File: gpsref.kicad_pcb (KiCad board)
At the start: 4 copper layers, 77.4 x 47.8 mm, 182 parts, among them J1 SMA, J11 Debug, J12 GPS_Snoop, J13 I2C_Snoop, J2 SMA, J3 SMA, J4 SMA, J5 U.Fl, J6 SMA, J7 USB_C_Receptacle_16P, Q1 AO3400A, Q2 AO3401A, T1 MABA-007159-000000, T2 MABA-007159-000000, U1 MAX-M10S, U12 74LVC1G125, U13 74CB3Q3306, U15 74LVC1G07, U2 TG5032CGN, U3 LMK05318BRGZR, U31 TMP117xxDRV, U4 STM32H503KBUx, U5 TPS82084SIL, U6 TPS82084SIL, U7 TPS7A8801RTJR, U9 TPS7A8801RTJR, Y1 32768Hz

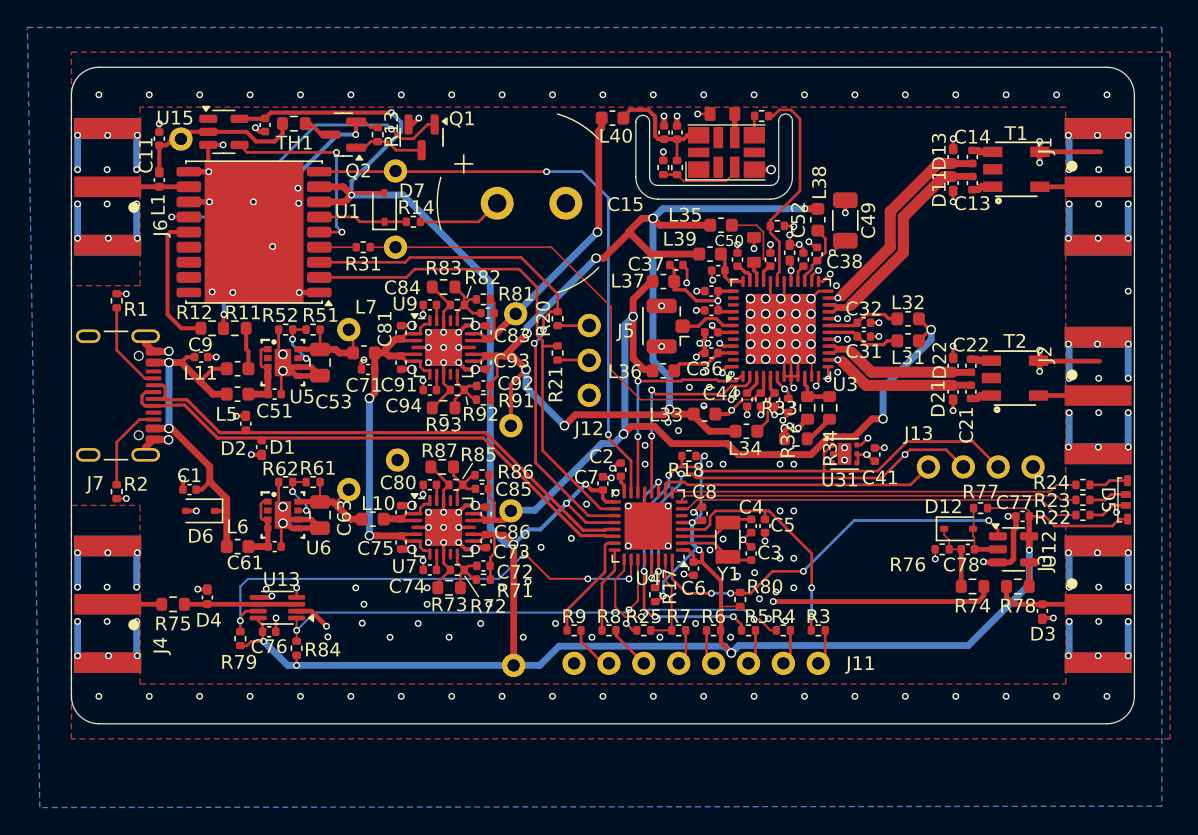
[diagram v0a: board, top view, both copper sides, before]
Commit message: Squeeze in a connector to break out GPS.
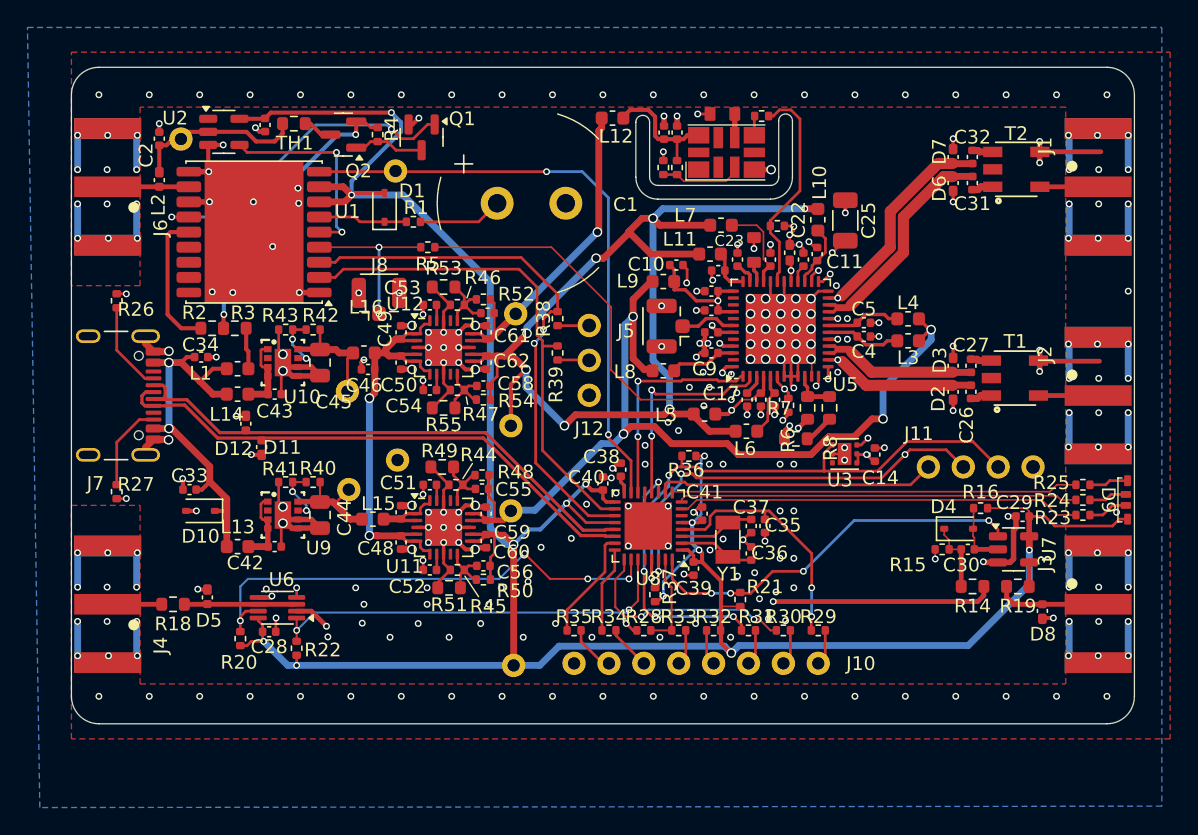
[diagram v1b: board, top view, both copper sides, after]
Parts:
- removed TP13: TestPoint_Probe, Parts:TestPoint
- added J8: U.Fl, Parts:U.FL_Hirose_U.FL-R-SMT-1_Vertical, F.Cu at (122.4, 93.0)
- moved R5 4.70 mm to (126.0, 89.2)
- moved TP5 4.50 mm to (120.1, 99.7)
- renumbered C15 to C1, C37 to C10, C38 to C11, C39 to C12, C40 to C13, C41 to C14, C42 to C15, C43 to C16, C44 to C17, C45 to C18, C46 to C19, C11 to C2, C47 to C20, C48 to C21, C52 to C22, C50 to C23, C56 to C24, C49 to C25, C21 to C26, C22 to C27, C76 to C28, C77 to C29, C12 to C3, C78 to C30, C13 to C31, C14 to C32, C1 to C33, C9 to C34, C5 to C35, C3 to C36, C4 to C37, C2 to C38, C6 to C39, C31 to C4, C7 to C40, C8 to C41, C61 to C42, C51 to C43, C63 to C44, C53 to C45, C71 to C46, C79 to C47, C75 to C48, C81 to C49, C32 to C5, C91 to C50, C80 to C51, C74 to C52, C84 to C53, C94 to C54, C85 to C55, C72 to C56, C82 to C57, C92 to C58, C86 to C59, C33 to C6, C73 to C60, C83 to C61, C93 to C62, C34 to C7, C35 to C8, C36 to C9, D7 to D1, D6 to D10, D1 to D11, D2 to D12, D21 to D2, D22 to D3, D12 to D4, D4 to D5, D11 to D6, D13 to D7, D3 to D8, D5 to D9, J11 to J10, J13 to J11, L11 to L1, L38 to L10, L39 to L11, L40 to L12, L6 to L13, L5 to L14, L10 to L15, L7 to L16, L1 to L2, L31 to L3, L32 to L4, L33 to L5, L34 to L6, L35 to L7, L36 to L8, L37 to L9, R14 to R1, R37 to R10, R38 to R11, R40 to R12, R39 to R13, R74 to R14, R76 to R15, R77 to R16, R75 to R18, R78 to R19, R12 to R2, R79 to R20, R80 to R21, R84 to R22, R22 to R23, R23 to R24, R24 to R25, R1 to R26, R2 to R27, R25 to R28, R3 to R29, R11 to R3, R4 to R30, R5 to R31, R6 to R32, R7 to R33, R8 to R34, R9 to R35, R18 to R36, R17 to R37, R20 to R38, R21 to R39, R13 to R4, R61 to R40, R62 to R41, R51 to R42, R52 to R43, R85 to R44, R72 to R45, R82 to R46, R92 to R47, R86 to R48, R87 to R49, R31 to R5, R71 to R50, R73 to R51, R81 to R52, R83 to R53, R91 to R54, R93 to R55, R32 to R6, R33 to R7, R34 to R8, R35 to R9, T2 to T1, T1 to T2, TP12 to TP1, TP14 to TP2, TP4 to TP3, TP6 to TP4, TP10 to TP6, U5 to U10, U7 to U11, U9 to U12, U15 to U2, U31 to U3, U2 to U4, U3 to U5, U13 to U6, U12 to U7, U4 to U8, U6 to U9
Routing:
- net GPSCLK: track 2.69 -> 12.2 mm, vias 0 -> 2
- net /Clocking/GPSCLKLO: track 39.7 -> 35.0 mm
- net /Power/3V6: track 7.22 -> 8.50 mm
- net GND: track 214.2 -> 214.4 mm, vias 300 -> 302

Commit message: Tweak positioning.
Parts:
- moved J7 0.50 mm to (102.8, 100.0)
- moved R26 0.50 mm to (103.8, 93.1)
- moved R27 0.50 mm to (103.8, 107.0)
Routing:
- net /CPU/USB_D-: track 40.0 -> 39.5 mm
- net /CPU/USB_D+: track 40.0 -> 39.5 mm
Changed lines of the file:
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@@
 	(footprint "Resistor_SMD:R_0402_1005Metric"
 		(layer "F.Cu")
-		(at 103.3 93.1 -90)
+		(at 103.8 93.1 -90)
 		(descr "Resistor SMD 0402 (1005 Metric), square (rectangular) end terminal, IPC-7351 nominal, (Body size source: IPC-SM-782 page 72, https://www.pcb-3d.com/wordpress/wp-content/uploads/ipc-sm-782a_amendment_1_and_2.pdf), generated with kicad-footprint-generator")
 		(tags "resistor")
@@
 	(footprint "Resistor_SMD:R_0402_1005Metric"
 		(layer "F.Cu")
-		(at 103.3 107 90)
+		(at 103.8 107 90)
 		(descr "Resistor SMD 0402 (1005 Metric), square (rectangular) end terminal, IPC-7351 nominal, (Body size source: IPC-SM-782 page 72, https://www.pcb-3d.com/wordpress/wp-content/uploads/ipc-sm-782a_amendment_1_and_2.pdf), generated with kicad-footprint-generator")
 		(tags "resistor")
@@
 		(locked yes)
 		(layer "F.Cu")
-		(at 102.3 100 -90)
+		(at 102.8 100 -90)
 		(descr "USB 2.0 Type C Receptacle, GCT, 16P, top mounted, horizontal, 5A: https://gct.co/files/drawings/usb4105.pdf")
 		(tags "USB C Type-C Receptacle SMD USB 2.0 16P 16C USB4105-15-A USB4105-15-A-060 USB4105-15-A-120 USB4105-GF-A USB4105-GF-A-060 USB4105-GF-A-120")
@@
 	)
 	(segment
-		(start 107.074228 103.2246)
-		(end 107.049628 103.2)
+		(start 107.574228 103.2246)
+		(end 107.549628 103.2)
 		(width 0.5)
 		(layer "F.Cu")
@@
 	)
 	(segment
-		(start 107.049628 103.2)
-		(end 105.98 103.2)
+		(start 107.549628 103.2)
+		(end 106.48 103.2)
 		(width 0.5)
 		(layer "F.Cu")
@@
 	)
 	(segment
-		(start 105.405 103.775)
-		(end 105.405 104.32)
+		(start 105.905 103.775)
+		(end 105.905 104.32)
 		(width 0.5)
 		(layer "F.Cu")
@@
 	)
 	(segment
-		(start 103.99 92.59)
-		(end 104 92.6)
+		(start 104.49 92.59)
+		(end 104.5 92.6)
 		(width 0.2)
 		(layer "F.Cu")
@@
 	)
 	(segment
-		(start 103.99 107.51)
-		(end 104 107.5)
+		(start 104.49 107.51)
+		(end 104.5 107.5)
 		(width 0.2)
 		(layer "F.Cu")
@@
 	)
 	(segment
-		(start 103.3 107.51)
-		(end 103.99 107.51)
+		(start 103.8 107.51)
+		(end 104.49 107.51)
 		(width 0.2)
 		(layer "F.Cu")
@@
 	)
 	(segment
-		(start 105.98 96.8)
-		(end 107.074997 96.8)
+		(start 106.48 96.8)
+		(end 107.574997 96.8)
 		(width 0.5)
 		(layer "F.Cu")
@@
 	)
 	(segment
-		(start 105.405 96.225)
-		(end 105.405 95.68)
+		(start 105.905 96.225)
+		(end 105.905 95.68)
 		(width 0.5)
 		(layer "F.Cu")
@@
 	)
 	(segment
-		(start 105.98 103.2)
-		(end 105.405 103.775)
+		(start 106.48 103.2)
+		(end 105.905 103.775)
 		(width 0.5)
 		(layer "F.Cu")
@@
 	)
 	(segment
-		(start 105.98 96.8)
-		(end 105.405 96.225)
+		(start 106.48 96.8)
+		(end 105.905 96.225)
 		(width 0.5)
 		(layer "F.Cu")
@@
 	)
 	(segment
-		(start 107.074997 96.8)
-		(end 107.1 96.774997)
+		(start 107.574997 96.8)
+		(end 107.6 96.774997)
 		(width 0.5)
 		(layer "F.Cu")
@@
 	)
 	(segment
-		(start 103.3 92.59)
-		(end 103.99 92.59)
+		(start 103.8 92.59)
+		(end 104.49 92.59)
 		(width 0.2)
 		(layer "F.Cu")
@@
 	)
 	(via
-		(at 107.074228 103.2246)
+		(at 107.574228 103.2246)
 		(size 0.7)
 		(drill 0.5)
@@
 	)
 	(via
-		(at 107.1 96.774997)
+		(at 107.6 96.774997)
 		(size 0.7)
 		(drill 0.5)
@@
 	)
 	(via
-		(at 104 92.6)
+		(at 104.5 92.6)
 		(size 0.5)
 		(drill 0.3)
@@
 	)
 	(via
-		(at 104 107.5)
+		(at 104.5 107.5)
 		(size 0.5)
 		(drill 0.3)
@@
 	)
 	(segment
-		(start 107.1 97.6)
-		(end 105.98 97.6)
+		(start 107.6 97.6)
+		(end 106.48 97.6)
 		(width 0.5)
 		(layer "F.Cu")
@@
 	)
 	(segment
-		(start 107.1 102.4)
-		(end 107.3 102.4)
+		(start 108 102.4)
+		(end 110.075 104.475)
+		(width 0.5)
+		(layer "F.Cu")
+		(net 2)
+	)
+	(segment
+		(start 110.075 104.475)
+		(end 110.075 106.275)
 		(width 0.5)
 		(layer "F.Cu")
@@
 	)
 	(segment
-		(start 109.375 98.975)
-		(end 110.3 99.9)
+		(start 107.1 102.4)
+		(end 108 102.4)
 		(width 0.5)
 		(layer "F.Cu")
@@
 	)
 	(segment
-		(start 108.4 97.2)
-		(end 108 97.6)
-		(width 0.3)
-		(layer "F.Cu")
-		(net 2)
-	)
-	(segment
-		(start 110.075 105.175)
-		(end 110.075 106.275)
+		(start 109.375 98.975)
+		(end 110.3 99.9)
 		(width 0.5)
 		(layer "F.Cu")
@@
 	)
 	(segment
-		(start 107.3 102.4)
-		(end 110.075 105.175)
-		(width 0.5)
+		(start 108.4 97.2)
+		(end 108 97.6)
+		(width 0.3)
 		(layer "F.Cu")
 		(net 2)
@@
 	)
 	(segment
-		(start 105.98 102.4)
-		(end 107.1 102.4)
+		(start 106.48 102.4)
+		(end 107.6 102.4)
 		(width 0.5)
 		(layer "F.Cu")
@@
 	)
 	(via
-		(at 107.1 97.6)
+		(at 107.6 97.6)
 		(size 0.7)
 		(drill 0.5)
@@
 	)
 	(via
-		(at 107.1 102.4)
+		(at 107.6 102.4)
 		(size 0.7)
 		(drill 0.5)
@@
 	)
 	(segment
-		(start 107.1 102.4)
-		(end 107.1 97.6)
+		(start 107.6 102.4)
+		(end 107.6 97.6)
 		(width 0.5)
 		(layer "B.Cu")
@@
 	)
 	(segment
-		(start 105.98 100.75)
-		(end 105.35 100.75)
+		(start 106.48 100.75)
+		(end 105.85 100.75)
 		(width 0.2395)
 		(layer "F.Cu")
@@
 	)
 	(segment
-		(start 105.405001 99.75)
-		(end 105.98 99.75)
+		(start 105.905001 99.75)
+		(end 106.48 99.75)
 		(width 0.2395)
 		(layer "F.Cu")
@@
 	)
 	(segment
-		(start 105.35 100.75)
-		(end 105.13425 100.53425)
+		(start 105.85 100.75)
+		(end 105.63425 100.53425)
 		(width 0.2395)
 		(layer "F.Cu")
@@
 	)
 	(segment
-		(start 106.842501 100.75)
-		(end 106.897751 100.69475)
+		(start 107.342501 100.75)
+		(end 107.397751 100.69475)
 		(width 0.2395)
 		(layer "F.Cu")
@@
 	)
 	(segment
-		(start 105.98 100.75)
-		(end 106.842501 100.75)
+		(start 106.48 100.75)
+		(end 107.342501 100.75)
 		(width 0.2395)
 		(layer "F.Cu")
@@
 	)
 	(segment
-		(start 105.13425 100.53425)
-		(end 105.13425 100.020751)
+		(start 108.24475 100.69475)
+		(end 107.397751 100.69475)
 		(width 0.2395)
 		(layer "F.Cu")
@@
 	)
 	(segment
-		(start 105.13425 100.020751)
-		(end 105.405001 99.75)
+		(start 105.63425 100.53425)
+		(end 105.63425 100.020751)
 		(width 0.2395)
 		(layer "F.Cu")
@@
 	)
 	(segment
-		(start 106.897751 100.69475)
-		(end 108.24475 100.69475)
+		(start 105.63425 100.020751)
+		(end 105.905001 99.75)
 		(width 0.2395)
 		(layer "F.Cu")
@@
 	)
 	(segment
-		(start 106.82575 100.07425)
-		(end 106.65 100.25)
+		(start 107.32575 100.07425)
+		(end 107.15 100.25)
 		(width 0.2395)
 		(layer "F.Cu")
@@
 	)
 	(segment
-		(start 106.842501 100.25)
-		(end 106.897751 100.30525)
+		(start 107.342501 100.25)
+		(end 107.397751 100.30525)
 		(width 0.2395)
 		(layer "F.Cu")
@@
 	)
 	(segment
-		(start 105.98 99.25)
-		(end 106.65 99.25)
+		(start 106.48 99.25)
+		(end 107.15 99.25)
+		(width 0.2395)
+		(layer "F.Cu")
+		(net 26)
+	)
+	(segment
+		(start 108.406084 100.30525)
+		(end 107.397751 100.30525)
 		(width 0.2395)
 		(layer "F.Cu")
@@
 	)
 	(segment
-		(start 106.82575 99.42575)
-		(end 106.82575 100.07425)
+		(start 107.32575 99.42575)
+		(end 107.32575 100.07425)
 		(width 0.2395)
 		(layer "F.Cu")
@@
 	)
 	(segment
-		(start 105.98 100.25)
-		(end 106.842501 100.25)
-		(width 0.2395)
-		(layer "F.Cu")
-		(net 26)
-	)
-	(segment
-		(start 106.897751 100.30525)
-		(end 108.406084 100.30525)
+		(start 106.48 100.25)
+		(end 107.342501 100.25)
 		(width 0.2395)
 		(layer "F.Cu")
@@
 	)
 	(segment
-		(start 106.65 99.25)
-		(end 106.82575 99.42575)
+		(start 107.15 99.25)
+		(end 107.32575 99.42575)
 		(width 0.2395)
 		(layer "F.Cu")
@@
 	)
 	(segment
-		(start 106.65 100.25)
-		(end 105.98 100.25)
+		(start 107.15 100.25)
+		(end 106.48 100.25)
 		(width 0.2395)
 		(layer "F.Cu")
@@
 	)
 	(segment
-		(start 105.98 98.75)
-		(end 105.35 98.75)
+		(start 106.48 98.75)
+		(end 105.85 98.75)
 		(width 0.2)
 		(layer "F.Cu")
@@
 	)
 	(segment
-		(start 103.3 96.7)
-		(end 103.3 93.61)
+		(start 103.8 96.7)
+		(end 103.8 93.61)
 		(width 0.2)
 		(layer "F.Cu")
@@
 	)
 	(segment
-		(start 105.35 98.75)
-		(end 103.3 96.7)
+		(start 105.85 98.75)
+		(end 103.8 96.7)
 		(width 0.2)
 		(layer "F.Cu")
@@
 	)
 	(segment
-		(start 105.98 101.75)
-		(end 104.95 101.75)
+		(start 106.48 101.75)
+		(end 105.45 101.75)
 		(width 0.2)
 		(layer "F.Cu")
@@
 	)
 	(segment
-		(start 104.95 101.75)
-		(end 103.3 103.4)
+		(start 105.45 101.75)
+		(end 103.8 103.4)
 		(width 0.2)
 		(layer "F.Cu")
@@
 	)
 	(segment
-		(start 103.3 103.4)
-		(end 103.3 106.49)
+		(start 103.8 103.4)
+		(end 103.8 106.49)
 		(width 0.2)
 		(layer "F.Cu")

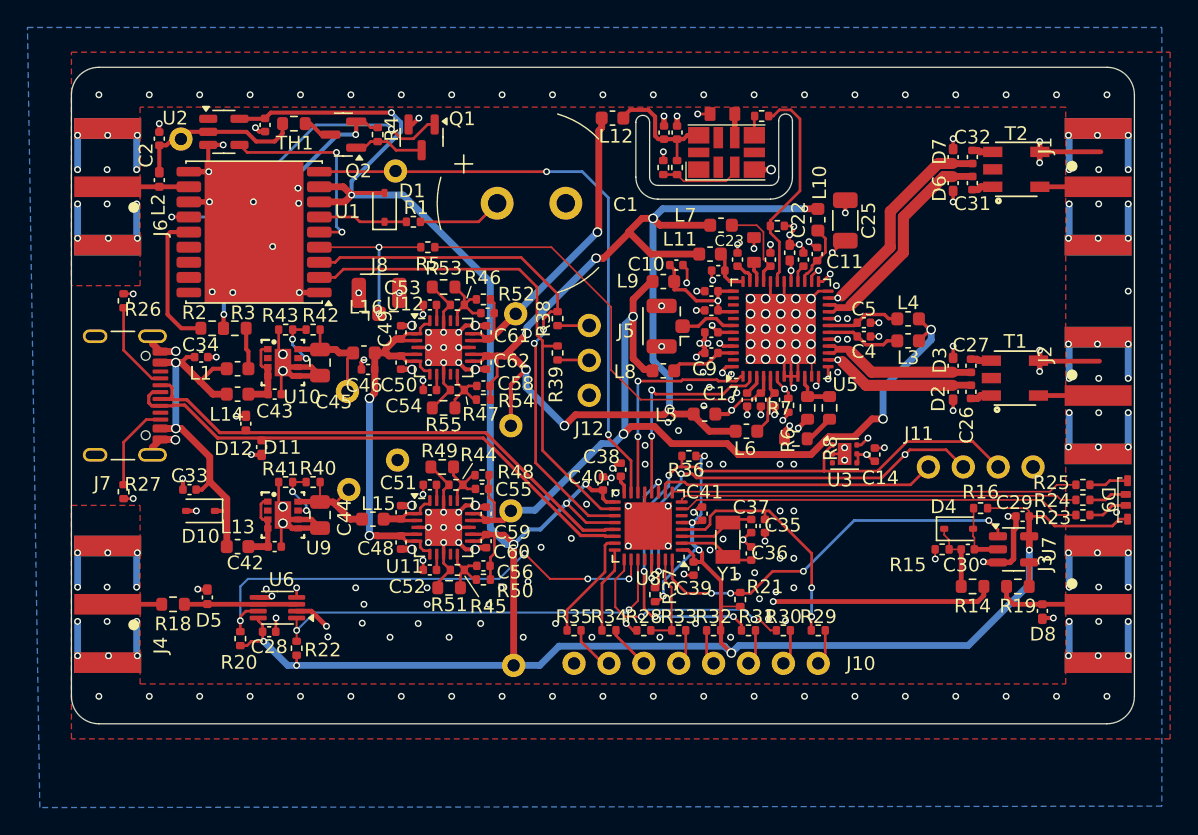
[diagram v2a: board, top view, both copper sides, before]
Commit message: Silkscreen passes DRC.  Also we renumbered everything.
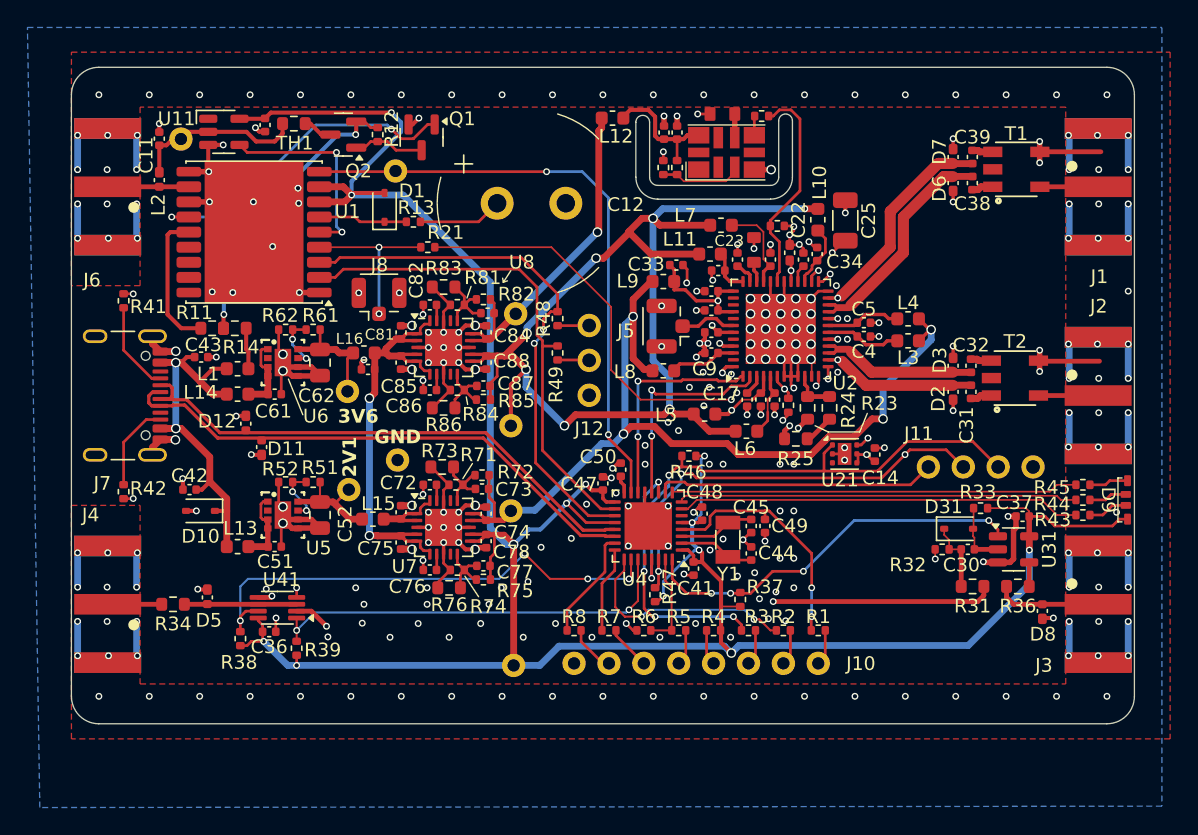
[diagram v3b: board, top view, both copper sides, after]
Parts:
- U11: renamed from U2; footprint Package_TO_SOT_SMD:SOT-23-5 -> Parts:SOT-23-5
- renumbered C13 to C1, C2 to C11, C1 to C12, C3 to C13, C15 to C2, C16 to C3, C26 to C31, C27 to C32, C10 to C33, C11 to C34, C12 to C35, C28 to C36, C29 to C37, C31 to C38, C32 to C39, C39 to C41, C33 to C42, C34 to C43, C36 to C44, C37 to C45, C40 to C47, C41 to C48, C35 to C49, C38 to C50, C42 to C51, C44 to C52, C43 to C61, C45 to C62, C47 to C71, C51 to C72, C55 to C73, C59 to C74, C48 to C75, C52 to C76, C56 to C77, C60 to C78, C49 to C81, C53 to C82, C57 to C83, C61 to C84, C50 to C85, C54 to C86, C58 to C87, C62 to C88, D4 to D31, R29 to R1, R2 to R11, R4 to R12, R1 to R13, R3 to R14, R30 to R2, R5 to R21, R6 to R22, R7 to R23, R8 to R24, R9 to R25, R12 to R26, R13 to R27, R10 to R28, R11 to R29, R31 to R3, R14 to R31, R15 to R32, R16 to R33, R18 to R34, R19 to R36, R21 to R37, R20 to R38, R22 to R39, R32 to R4, R26 to R41, R27 to R42, R23 to R43, R24 to R44, R25 to R45, R36 to R46, R37 to R47, R38 to R48, R39 to R49, R33 to R5, R40 to R51, R41 to R52, R28 to R6, R42 to R61, R43 to R62, R34 to R7, R44 to R71, R48 to R72, R49 to R73, R45 to R74, R50 to R75, R51 to R76, R35 to R8, R46 to R81, R52 to R82, R53 to R83, R47 to R84, R54 to R85, R55 to R86, T2 to T1, T1 to T2, U5 to U2, U3 to U21, U4 to U3, U7 to U31, U8 to U4, U6 to U41, U9 to U5, U10 to U6, U11 to U7, U12 to U8
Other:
- board text added: "2V1"
- board text added: "3V6"
- board text added: "GND"
